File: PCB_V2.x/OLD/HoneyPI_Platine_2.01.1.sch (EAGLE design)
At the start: 76 parts

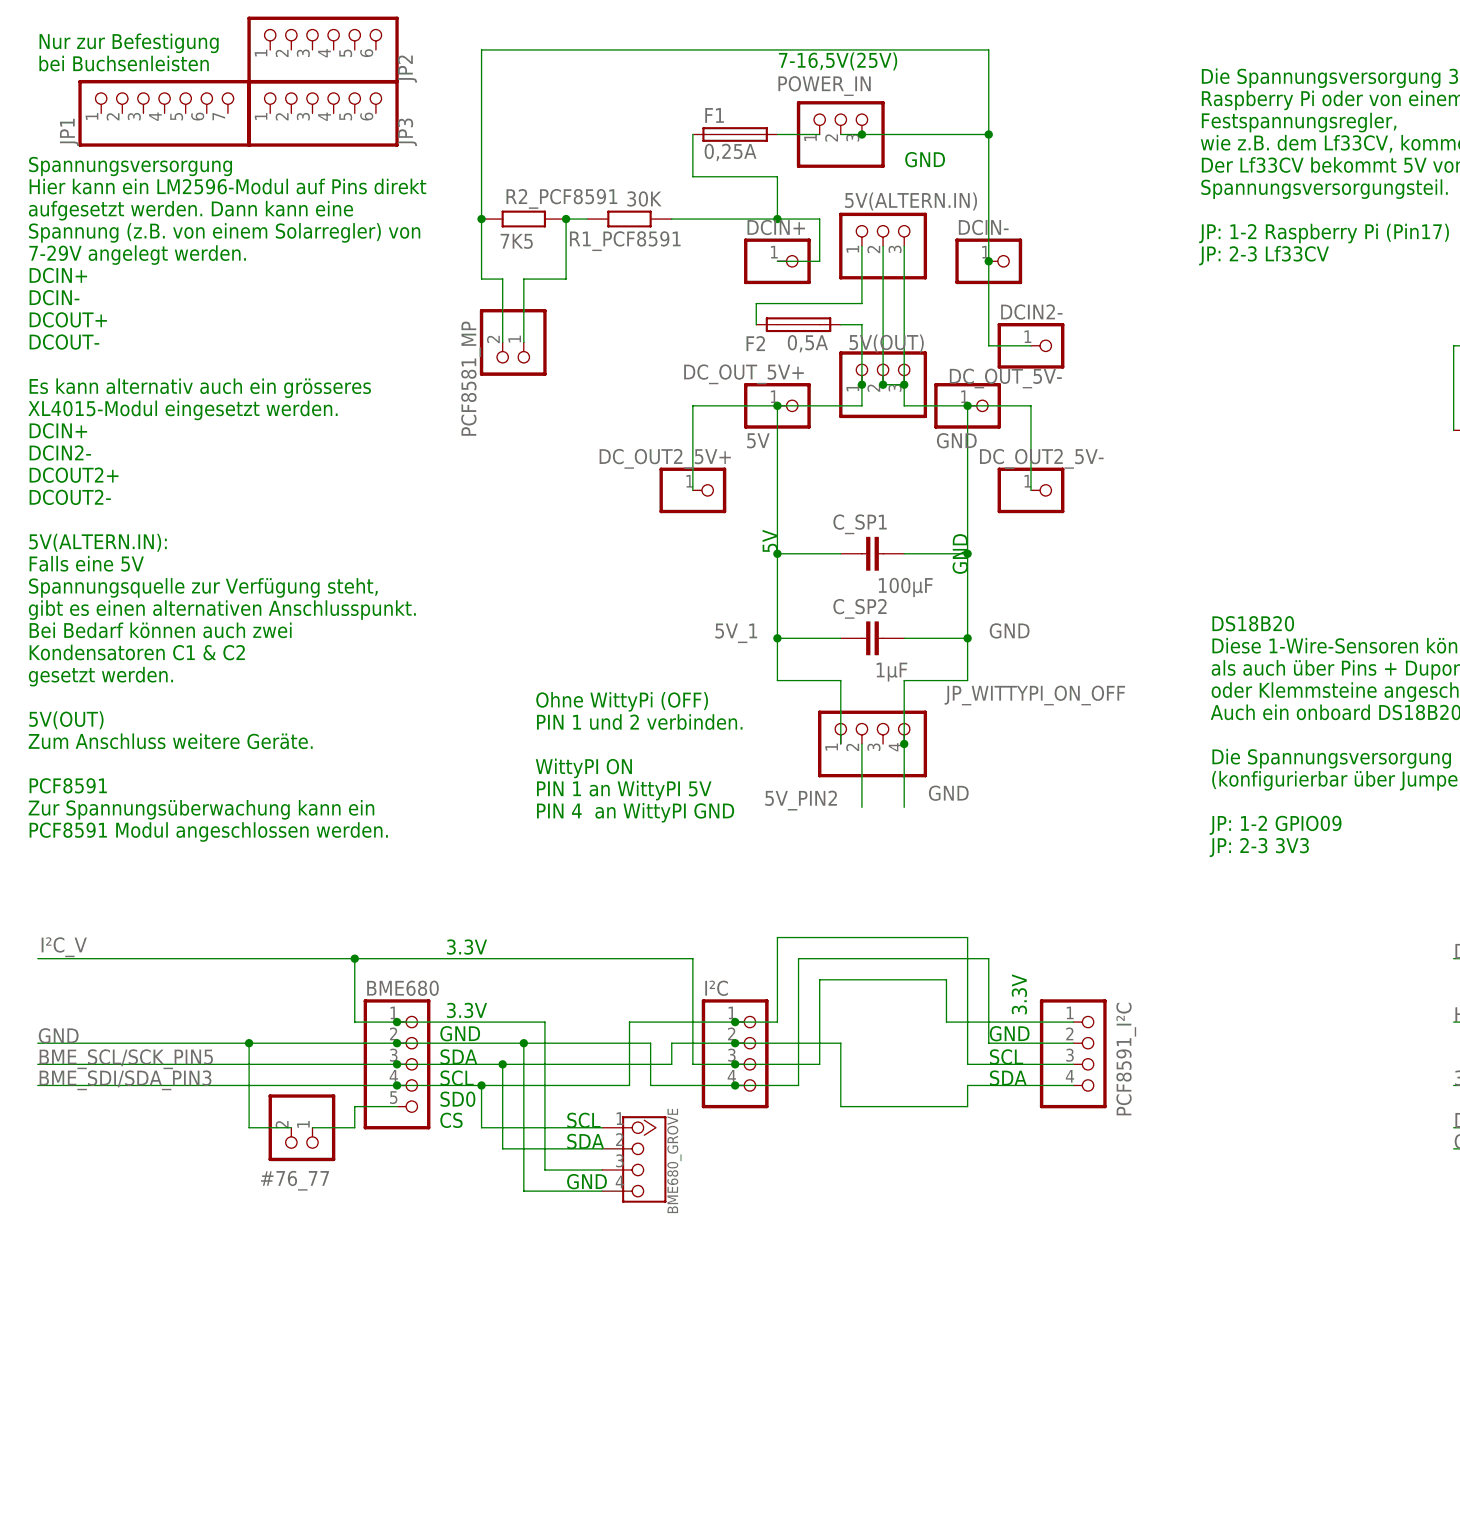
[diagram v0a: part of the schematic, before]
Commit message: New releases
Fix BME680_GROVE Pinout on the main board
Some corrections on the sensor board
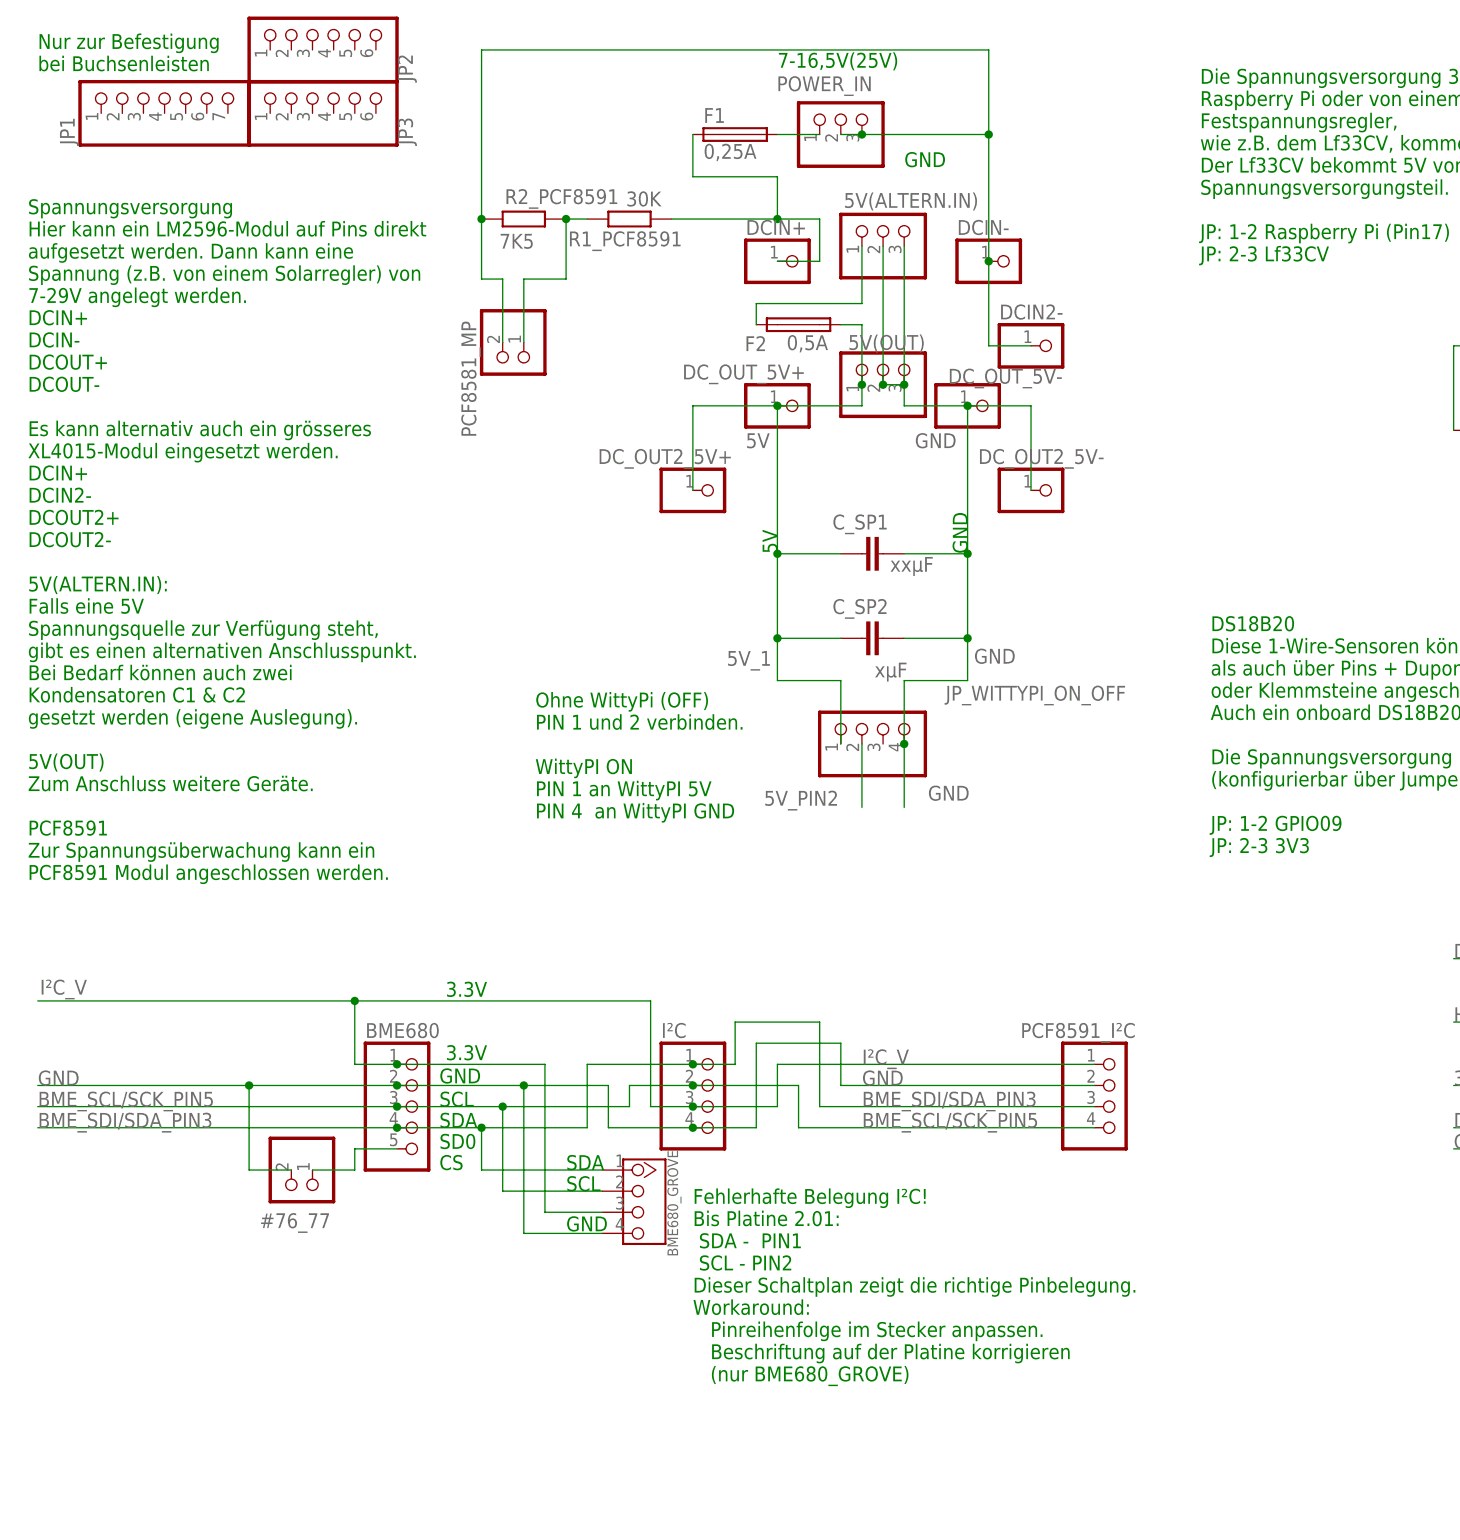
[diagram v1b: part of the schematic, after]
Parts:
- C_SP1: value 100µF -> xxµF
- C_SP2: value 1µF -> xµF
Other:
- note added: "Fehlerhafte Belegung I²C! Bis Platine 2.01: SDA - PIN1 SCL - PIN2 Dieser Schaltplan zeigt die richtige Pinbelegung. Workaround: Pinreihenfolge im Stecker anpassen. Beschriftung auf der Platine korrigieren (nur BME680_GROVE)"
- moved on the sheet: #76_77, BME680, BME680_GROVE, I²C, PCF8591_I²C
